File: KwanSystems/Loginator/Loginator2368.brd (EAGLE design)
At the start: 61 x 38.1 mm, 71 parts, among them J001 USBSMD, J002 M01PTH, J301 JST 2mm, J401 M06, J402 M04, J403 M10, J404 M06, J406 M12PTH, J701 MICROSD-SOCKET, Q050 PMOS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

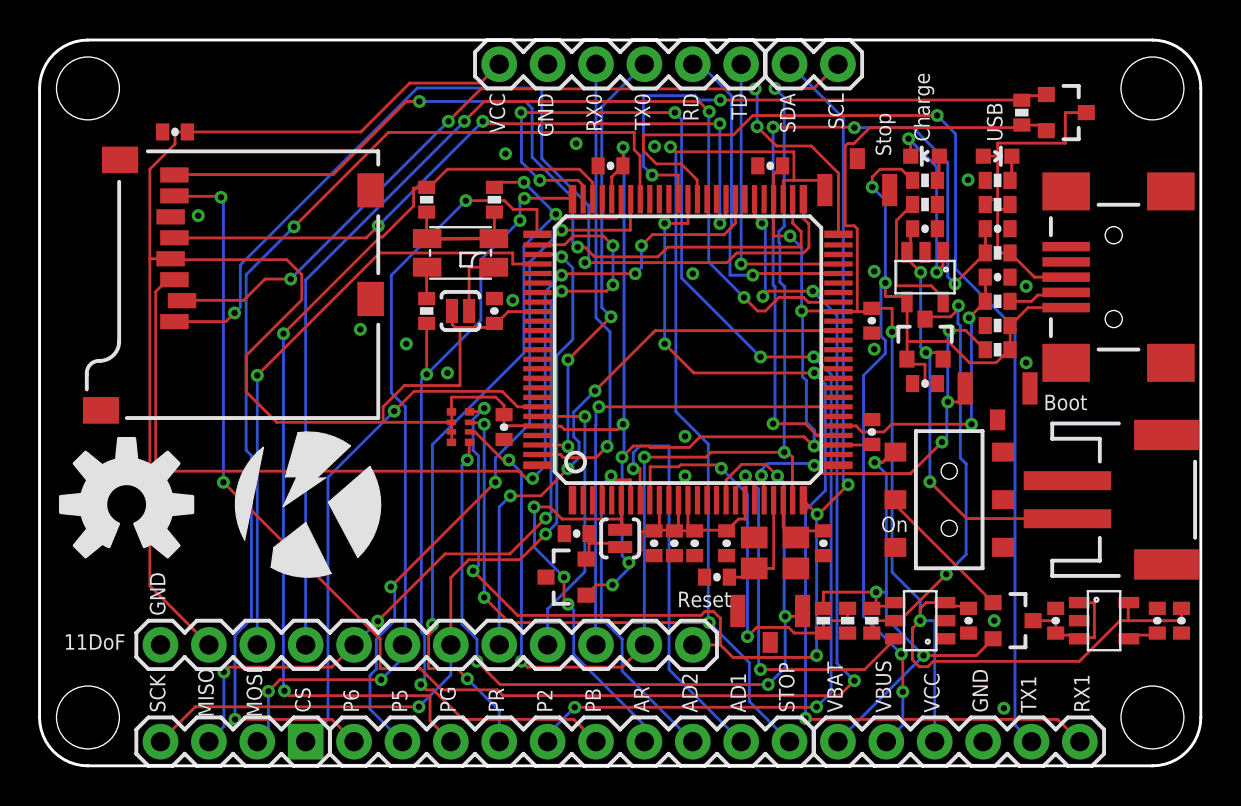
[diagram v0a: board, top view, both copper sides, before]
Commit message: Reorganized docs for ARM. Added engine rooms with AD magnetic couplers instead of optocouplers.
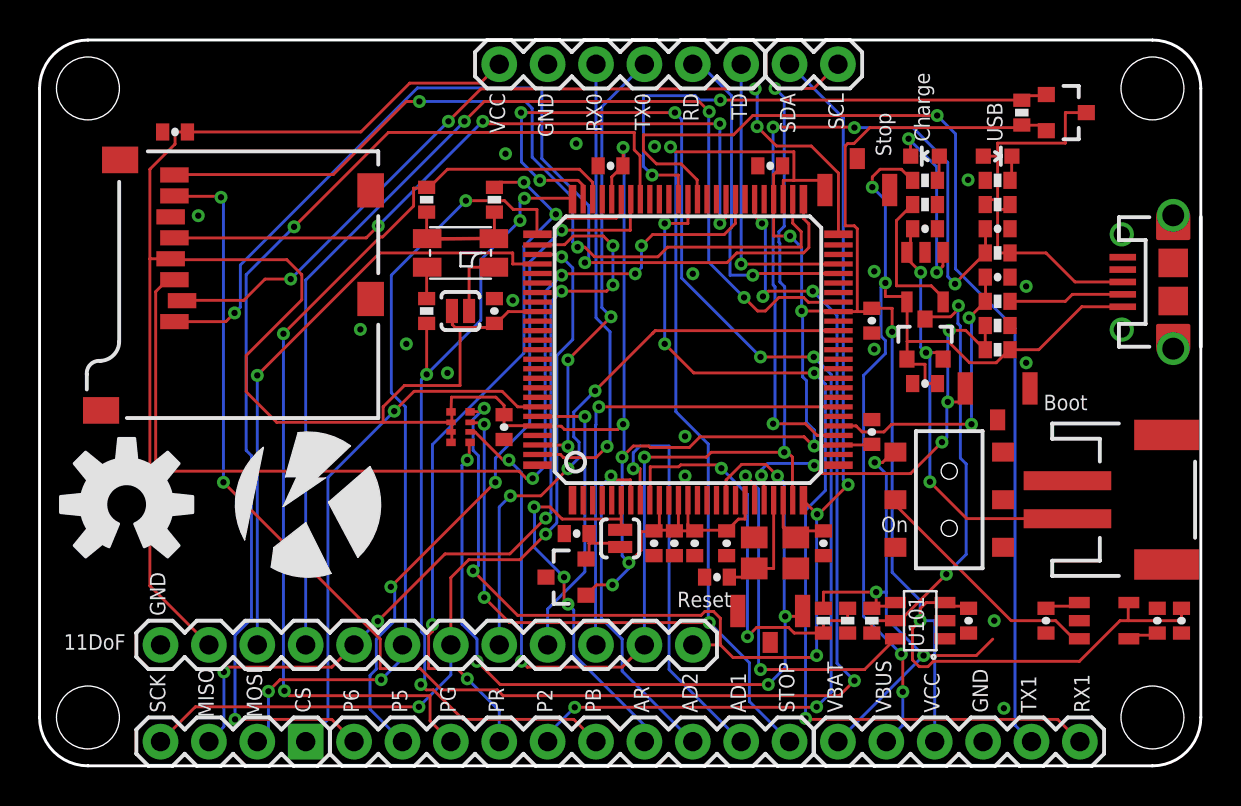
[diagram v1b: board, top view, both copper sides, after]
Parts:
- removed Q201: PMOS, SparkFun:SOT23-3
- J001: value USBSMD -> USB_MICROB_JSTFCI; device SparkFun:USB-MINIB -> KwanSystems:USB-MICROB-CONN-09505
- R010: value 10k -> 24k
- R011: value 100k -> 39k
- U101: value 100V/V -> MAX4173
- Y401: value 12M -> TSX-3225
- moved J001 4.58 mm to (61.0, 25.4), turned to 90 degrees
- moved C201 0.51 mm to (52.8, 7.62), turned to 270 degrees
- turned Y401 to 0 degrees
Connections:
- removed net N$10: Q201.1, S201.2
- removed net RAW: C201.1, Q201.3, U201.1, U201.3
- new net EN: S201.2, U201.3
- net CONN_D+: now also J001.3; no longer J001.D+
- net CONN_D-: now also J001.2; no longer J001.D-
- net GND: now also J001.5, J001.P1, J001.P2, J001.P3, J001.P4, J001.P5, J001.P6, R011.2; no longer J001.GND, R011.1
- net USB_ON: now also R011.1
- net VBUS: now also J001.1; no longer J001.VBUS, R011.2
- net VIN-: now also C201.1, U201.1; no longer Q201.2
- net XTAL1: now also Y401.1; no longer Y401.3
- net XTAL2: now also Y401.3; no longer Y401.1
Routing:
- net EN: track 0.00 -> 12.9 mm
- net N$10: track 7.53 -> 0.00 mm
- net RAW: track 6.74 -> 0.00 mm
- net CONN_D+: track 7.34 -> 10.4 mm
- net CONN_D-: track 3.15 -> 6.08 mm
- net VBUS: track 53.0 -> 55.2 mm
- net VIN-: track 29.4 -> 31.3 mm
- net USB_ON: track 22.2 -> 23.5 mm

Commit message: Split up
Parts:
- removed S201: SPDT, SparkFun:AYZ0202
- added S202: AYZ0202, KwanSystems:AYZ0202
- JP1, JP2, JP3, JP4: value STAND-OFF -> STANDOFF; device SparkFun:STAND-OFF -> KwanSystems:STANDOFF
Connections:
- net EN: now also S202.2; no longer S201.2
- net GND: now also JP1.P$1, JP2.P$1, JP3.P$1, JP4.P$1, S202.3; no longer S201.1
- net VIN-: now also S202.1; no longer S201.3
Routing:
- net VIN-: track 31.3 -> 29.0 mm
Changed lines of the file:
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@@
 <?xml version="1.0" encoding="utf-8"?>
 <!DOCTYPE eagle SYSTEM "eagle.dtd">
-<eagle version="6.2">
+<eagle version="6.6.0">
 <drawing>
 <settings>
@@
 </class>
 </classes>
-<designrules>
+<designrules name="default">
 <description language="de">&lt;b&gt;EAGLE Design Rules&lt;/b&gt;
 &lt;p&gt;
@@
 <attribute name="DIGIKEY" value="P33.0LCT-ND" x="20.32" y="29.718" size="1.778" layer="27" rot="R90" display="off"/>
 </element>
-<element name="JP1" library="SparkFun" package="STAND-OFF" value="STAND-OFF" x="2.54" y="2.54">
+<element name="JP1" library="KwanSystems" package="STANDOFF" value="STANDOFF" x="2.54" y="2.54">
 <attribute name="DIGIKEY" value="$NOPART" x="2.54" y="2.54" size="1.778" layer="27" display="off"/>
 </element>
-<element name="JP2" library="SparkFun" package="STAND-OFF" value="STAND-OFF" x="58.42" y="2.54">
+<element name="JP2" library="KwanSystems" package="STANDOFF" value="STANDOFF" x="58.42" y="2.54">
 <attribute name="DIGIKEY" value="$NOPART" x="58.42" y="2.54" size="1.778" layer="27" display="off"/>
 </element>
-<element name="JP3" library="SparkFun" package="STAND-OFF" value="STAND-OFF" x="2.54" y="35.56">
+<element name="JP3" library="KwanSystems" package="STANDOFF" value="STANDOFF" x="2.54" y="35.56">
 <attribute name="DIGIKEY" value="$NOPART" x="2.54" y="35.56" size="1.778" layer="27" display="off"/>
 </element>
-<element name="JP4" library="SparkFun" package="STAND-OFF" value="STAND-OFF" x="58.42" y="35.56">
+<element name="JP4" library="KwanSystems" package="STANDOFF" value="STANDOFF" x="58.42" y="35.56">
 <attribute name="DIGIKEY" value="$NOPART" x="58.42" y="35.56" size="1.778" layer="27" display="off"/>
 </element>
@@
 <attribute name="DIGIKEY" value="445-7395-1-ND" x="46.482" y="20.066" size="1.778" layer="27" rot="R180" display="off"/>
 </element>
-<element name="S201" library="SparkFun" package="AYZ0202" value="SPDT" x="47.752" y="13.97" smashed="yes" rot="R90">
-<attribute name="NAME" x="46.609" y="11.43" size="0.4064" layer="51" rot="R90"/>
-<attribute name="VALUE" x="46.609" y="14.478" size="0.4064" layer="27" rot="R90"/>
-<attribute name="DIGIKEY" value="401-2013-1-ND" x="47.752" y="13.97" size="1.778" layer="27" rot="R90" display="off"/>
-</element>
 <element name="C204" library="SparkFun" package="0402-CAP" value="100nF" x="58.674" y="7.62" smashed="yes" rot="R90">
 <attribute name="NAME" x="58.9915" y="8.255" size="0.4064" layer="51" rot="R90"/>
@@
 <element name="Y401" library="KwanSystems" package="CRYSTAL_SMD" value="TSX-3225" x="38.608" y="11.176"/>
 <element name="U101" library="KwanSystems" package="SOT-23-6" value="MAX4173" x="46.228" y="7.62" rot="R90"/>
+<element name="S202" library="KwanSystems" package="AYZ0202" value="AYZ0202" x="47.752" y="13.97" rot="R90"/>
 </elements>
 <signals>
@@
 <contactref element="R101" pad="1"/>
 <contactref element="C103" pad="2"/>
-<contactref element="S201" pad="1"/>
 <contactref element="C471" pad="2"/>
 <contactref element="C496" pad="2"/>
@@
 <contactref element="U401" pad="83"/>
 <contactref element="U401" pad="97"/>
+<contactref element="JP3" pad="P$1"/>
+<contactref element="JP4" pad="P$1"/>
+<contactref element="JP1" pad="P$1"/>
+<contactref element="JP2" pad="P$1"/>
+<contactref element="S202" pad="3"/>
 </signal>
 <signal name="USBD+">
@@
 </signal>
 <signal name="VIN-">
-<contactref element="S201" pad="3"/>
 <contactref element="J404" pad="1"/>
 <contactref element="R103" pad="2"/>
@@
 <wire x1="41.91" y1="1.2954" x2="46.4058" y2="5.7912" width="0.1524" layer="16"/>
 <wire x1="41.91" y1="1.27" x2="41.91" y2="1.2954" width="0.1524" layer="16"/>
-<wire x1="44.45" y1="15.3162" x2="43.8404" y2="15.9258" width="0.1524" layer="16"/>
 <wire x1="44.45" y1="7.747" x2="44.45" y2="9.1186" width="0.1524" layer="16"/>
-<wire x1="44.45" y1="9.1186" x2="44.45" y2="15.3162" width="0.1524" layer="16"/>
 <wire x1="46.4058" y1="5.7912" x2="44.45" y2="7.747" width="0.1524" layer="16"/>
-<wire x1="44.9072" y1="16.4592" x2="44.927" y2="16.47" width="0.1524" layer="1"/>
 <wire x1="44.45" y1="9.1186" x2="43.9166" y2="9.1186" width="0.1524" layer="16"/>
 <via x="46.4058" y="5.7912" extent="1-16" drill="0.3302"/>
-<via x="43.8404" y="15.9258" extent="1-16" drill="0.3302"/>
+<via x="43.9674" y="12.7508" extent="1-16" drill="0.3302"/>
 <via x="43.9166" y="9.1186" extent="1-16" drill="0.3302"/>
-<wire x1="43.8404" y1="15.9258" x2="44.2468" y2="15.9258" width="0.1524" layer="1"/>
-<wire x1="44.2468" y1="15.9258" x2="44.45" y2="16.129" width="0.1524" layer="1"/>
-<wire x1="44.45" y1="16.129" x2="44.586" y2="16.129" width="0.1524" layer="1"/>
-<wire x1="44.586" y1="16.129" x2="44.927" y2="16.47" width="0.1524" layer="1"/>
 <wire x1="43.9166" y1="9.1186" x2="43.9166" y2="8.4986" width="0.1524" layer="1"/>
 <wire x1="43.9166" y1="8.4986" x2="43.688" y2="8.27" width="0.1524" layer="1"/>
@@
 <contactref element="U101" pad="4"/>
 <wire x1="44.638" y1="8.57" x2="44.928" y2="8.57" width="0.1524" layer="1"/>
+<contactref element="S202" pad="1"/>
+<wire x1="43.9674" y1="12.7508" x2="44.927" y2="12.7508" width="0.1524" layer="1"/>
+<wire x1="44.927" y1="12.7508" x2="44.927" y2="11.47" width="0.1524" layer="1"/>
+<wire x1="44.45" y1="9.1186" x2="44.45" y2="12.2682" width="0.1524" layer="16"/>
+<wire x1="44.45" y1="12.2682" x2="43.9674" y2="12.7508" width="0.1524" layer="16"/>
 <wire x1="50.038" y1="6.6548" x2="52.832" y2="8.27" width="0" layer="19" extent="1-1"/>
 </signal>
@@
 <wire x1="54.58" y1="6.67" x2="54.61" y2="6.64" width="0.1524" layer="1"/>
 <wire x1="54.61" y1="6.64" x2="54.61" y2="6.604" width="0.1524" layer="1"/>
-<contactref element="S201" pad="2"/>
 <wire x1="44.9326" y1="13.6906" x2="51.0032" y2="7.62" width="0.1524" layer="1"/>
 <wire x1="44.9326" y1="13.97" x2="44.9326" y2="13.6906" width="0.1524" layer="1"/>
@@
 <wire x1="53.34" y1="7.62" x2="54.29" y2="6.67" width="0.1524" layer="1"/>
 <wire x1="54.29" y1="6.67" x2="54.58" y2="6.67" width="0.1524" layer="1"/>
+<contactref element="S202" pad="2"/>
 </signal>
 </signals>

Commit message: Pushing back
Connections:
- net PWMR$ renamed PWMR
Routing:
- net VIN-: track 29.0 -> 38.5 mm
- net VCC: track 246.2 -> 247.5 mm
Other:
- board text added: "01 Apr 2016"
- board text added: "Loginator4078"
- board text removed: "13 Apr 2012"
- board text removed: "Loginator2368"
